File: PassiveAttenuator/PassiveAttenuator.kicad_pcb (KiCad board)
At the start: 2 copper layers, 15 x 100 mm, 6 parts, among them J1 AudioJack2_SwitchT, J2 AudioJack2_SwitchT, J3 AudioJack2_SwitchT, J4 AudioJack2_SwitchT

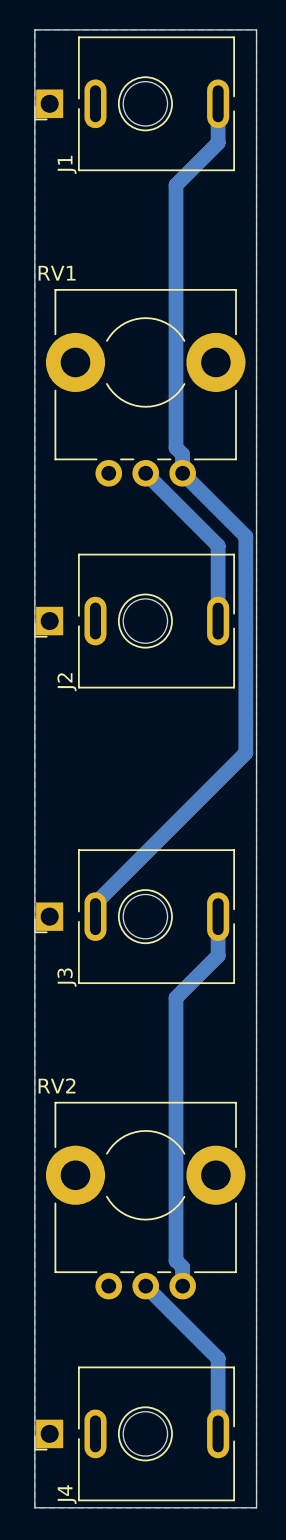
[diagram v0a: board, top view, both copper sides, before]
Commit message: Moved potentiometers to top.
Add top layer gnd pour
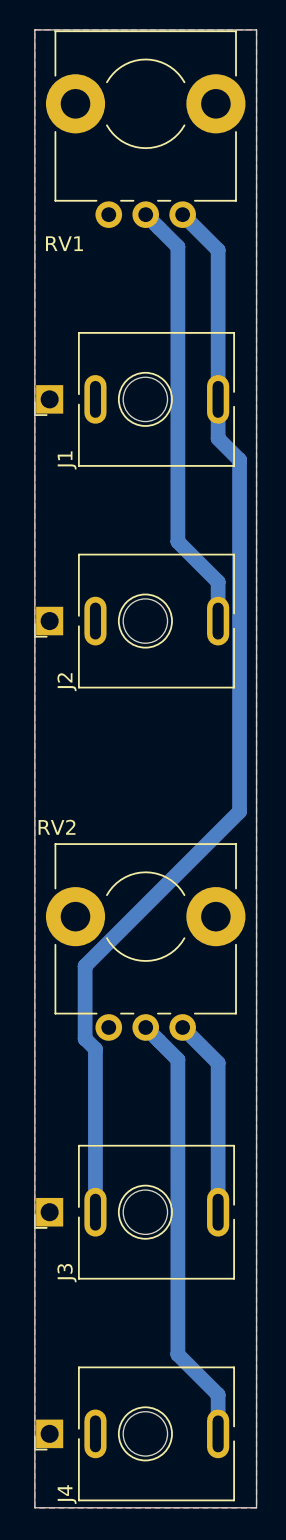
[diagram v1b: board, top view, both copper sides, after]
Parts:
- moved J1 20.0 mm to (151.0, 75.0)
- moved J3 20.0 mm to (151.0, 130.0)
- moved RV1 17.5 mm to (160.0, 62.5)
- moved RV2 17.5 mm to (160.0, 117.5)
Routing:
- net Net-(J4-PadT): track 12.0 -> 29.5 mm
- net Net-(J2-PadT): track 12.0 -> 29.5 mm
- net Net-(J3-PadT): track 26.4 -> 13.5 mm
- net Net-(J1-PadT): track 62.4 -> 73.7 mm
- added copper zone on F.Cu, net GND
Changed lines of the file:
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@@
     (thickness 1.6)
     (drawings 4)
-    (tracks 18)
+    (tracks 21)
     (zones 0)
     (modules 6)
@@
     (solder_mask_min_width 0.25)
     (aux_axis_origin 0 0)
-    (visible_elements FFFFFF7F)
+    (visible_elements 7FFFFFFF)
     (pcbplotparams
       (layerselection 0x010fc_ffffffff)
@@
   )
   (module _NTSFootprints:Jack_3.5mm_QingPu_WQP-PJ398SM_Vertical_CenterHole_OvalPads (layer F.Cu)
-    (at 151 55 90)
+    (at 151 75 90)
     (descr "TRS 3.5mm, vertical, Thonkiconn, PCB mount, (http://www.qingpu-electronics.com/en/products/WQP-PJ398SM-362.html)")
     (tags "WQP-PJ398SM WQP-PJ301M-12 TRS 3.5mm mono vertical jack thonkiconn qingpu")
@@
   )
   (module _NTSFootprints:Jack_3.5mm_QingPu_WQP-PJ398SM_Vertical_CenterHole_OvalPads (layer F.Cu)
-    (at 151 110 90)
+    (at 151 130 90)
     (descr "TRS 3.5mm, vertical, Thonkiconn, PCB mount, (http://www.qingpu-electronics.com/en/products/WQP-PJ398SM-362.html)")
     (tags "WQP-PJ398SM WQP-PJ301M-12 TRS 3.5mm mono vertical jack thonkiconn qingpu")
@@
   )
   (module _NTSFootprints:Potentiometer_Alps_RK09L_Plated_Mount_Holes (layer F.Cu)
-    (at 160 80 90)
+    (at 160 62.5 90)
     (descr "Potentiometer, horizontally mounted, Omeg PC16PU, Omeg PC16PU, Omeg PC16PU, Vishay/Spectrol 248GJ/249GJ Single, Vishay/Spectrol 248GJ/249GJ Single, Vishay/Spectrol 248GJ/249GJ Single, Vishay/Spectrol 248GH/249GH Single, Vishay/Spectrol 148/149 Single, Vishay/Spectrol 148/149 Single, Vishay/Spectrol 148/149 Single, Vishay/Spectrol 148A/149A Single with mounting plates, Vishay/Spectrol 148/149 Double, Vishay/Spectrol 148A/149A Double with mounting plates, Piher PC-16 Single, Piher PC-16 Single, Piher PC-16 Single, Piher PC-16SV Single, Piher PC-16 Double, Piher PC-16 Triple, Piher T16H Single, Piher T16L Single, Piher T16H Double, Alps RK163 Single, Alps RK163 Double, Alps RK097 Single, Alps RK097 Double, Bourns PTV09A-2 Single with mounting sleve Single, Bourns PTV09A-1 with mounting sleve Single, Bourns PRS11S Single, Alps RK09K Single with mounting sleve Single, Alps RK09K with mounting sleve Single, Alps RK09L Single, Alps RK09L Single, http://www.alps.com/prod/info/E/HTML/Potentiometer/RotaryPotentiometers/RK09L/RK09L1140A5E.html")
     (tags "Potentiometer horizontal  Omeg PC16PU  Omeg PC16PU  Omeg PC16PU  Vishay/Spectrol 248GJ/249GJ Single  Vishay/Spectrol 248GJ/249GJ Single  Vishay/Spectrol 248GJ/249GJ Single  Vishay/Spectrol 248GH/249GH Single  Vishay/Spectrol 148/149 Single  Vishay/Spectrol 148/149 Single  Vishay/Spectrol 148/149 Single  Vishay/Spectrol 148A/149A Single with mounting plates  Vishay/Spectrol 148/149 Double  Vishay/Spectrol 148A/149A Double with mounting plates  Piher PC-16 Single  Piher PC-16 Single  Piher PC-16 Single  Piher PC-16SV Single  Piher PC-16 Double  Piher PC-16 Triple  Piher T16H Single  Piher T16L Single  Piher T16H Double  Alps RK163 Single  Alps RK163 Double  Alps RK097 Single  Alps RK097 Double  Bourns PTV09A-2 Single with mounting sleve Single  Bourns PTV09A-1 with mounting sleve Single  Bourns PRS11S Single  Alps RK09K Single with mounting sleve Single  Alps RK09K with mounting sleve Single  Alps RK09L Single  Alps RK09L Single")
-    (fp_text reference RV1 (at 13.5 -8.5 180) (layer F.SilkS)
-      (effects (font (size 1 1) (thickness 0.15)))
-    )
-    (fp_text value R_POT (at 13.5 -4 180) (layer F.Fab) hide
+    (fp_text reference RV1 (at -2 -8 180) (layer F.SilkS)
+      (effects (font (size 1 1) (thickness 0.15)))
+    )
+    (fp_text value R_POT (at 8 -2.5 180) (layer F.Fab) hide
       (effects (font (size 1 1) (thickness 0.15)))
     )
@@
   )
   (module _NTSFootprints:Potentiometer_Alps_RK09L_Plated_Mount_Holes (layer F.Cu)
-    (at 160 135 90)
+    (at 160 117.5 90)
     (descr "Potentiometer, horizontally mounted, Omeg PC16PU, Omeg PC16PU, Omeg PC16PU, Vishay/Spectrol 248GJ/249GJ Single, Vishay/Spectrol 248GJ/249GJ Single, Vishay/Spectrol 248GJ/249GJ Single, Vishay/Spectrol 248GH/249GH Single, Vishay/Spectrol 148/149 Single, Vishay/Spectrol 148/149 Single, Vishay/Spectrol 148/149 Single, Vishay/Spectrol 148A/149A Single with mounting plates, Vishay/Spectrol 148/149 Double, Vishay/Spectrol 148A/149A Double with mounting plates, Piher PC-16 Single, Piher PC-16 Single, Piher PC-16 Single, Piher PC-16SV Single, Piher PC-16 Double, Piher PC-16 Triple, Piher T16H Single, Piher T16L Single, Piher T16H Double, Alps RK163 Single, Alps RK163 Double, Alps RK097 Single, Alps RK097 Double, Bourns PTV09A-2 Single with mounting sleve Single, Bourns PTV09A-1 with mounting sleve Single, Bourns PRS11S Single, Alps RK09K Single with mounting sleve Single, Alps RK09K with mounting sleve Single, Alps RK09L Single, Alps RK09L Single, http://www.alps.com/prod/info/E/HTML/Potentiometer/RotaryPotentiometers/RK09L/RK09L1140A5E.html")
     (tags "Potentiometer horizontal  Omeg PC16PU  Omeg PC16PU  Omeg PC16PU  Vishay/Spectrol 248GJ/249GJ Single  Vishay/Spectrol 248GJ/249GJ Single  Vishay/Spectrol 248GJ/249GJ Single  Vishay/Spectrol 248GH/249GH Single  Vishay/Spectrol 148/149 Single  Vishay/Spectrol 148/149 Single  Vishay/Spectrol 148/149 Single  Vishay/Spectrol 148A/149A Single with mounting plates  Vishay/Spectrol 148/149 Double  Vishay/Spectrol 148A/149A Double with mounting plates  Piher PC-16 Single  Piher PC-16 Single  Piher PC-16 Single  Piher PC-16SV Single  Piher PC-16 Double  Piher PC-16 Triple  Piher T16H Single  Piher T16L Single  Piher T16H Double  Alps RK163 Single  Alps RK163 Double  Alps RK097 Single  Alps RK097 Double  Bourns PTV09A-2 Single with mounting sleve Single  Bourns PTV09A-1 with mounting sleve Single  Bourns PRS11S Single  Alps RK09K Single with mounting sleve Single  Alps RK09K with mounting sleve Single  Alps RK09L Single  Alps RK09L Single")
@@
   (gr_line (start 150 150) (end 165 150) (layer Edge.Cuts) (width 0.05))
   (gr_line (start 150 50) (end 150 150) (layer Edge.Cuts) (width 0.05))
-  (segment (start 160 78.727208) (end 160 80) (width 1) (layer B.Cu) (net 1))
-  (segment (start 159.549999 78.277207) (end 160 78.727208) (width 1) (layer B.Cu) (net 1))
-  (segment (start 159.549999 60.500001) (end 159.549999 78.277207) (width 1) (layer B.Cu) (net 1))
-  (segment (start 162.4 57.65) (end 159.549999 60.500001) (width 1) (layer B.Cu) (net 1))
-  (segment (start 162.4 55) (end 162.4 57.65) (width 1) (layer B.Cu) (net 1))
-  (segment (start 154.1 109.1) (end 154.1 110) (width 1) (layer B.Cu) (net 1))
-  (segment (start 164.27499 98.92501) (end 154.1 109.1) (width 1) (layer B.Cu) (net 1))
-  (segment (start 164.27499 84.27499) (end 164.27499 98.92501) (width 1) (layer B.Cu) (net 1))
-  (segment (start 160 80) (end 164.27499 84.27499) (width 1) (layer B.Cu) (net 1))
-  (segment (start 162.4 84.9) (end 157.5 80) (width 1) (layer B.Cu) (net 5))
-  (segment (start 162.4 90) (end 162.4 84.9) (width 1) (layer B.Cu) (net 5))
-  (segment (start 162.4 112.65) (end 162.4 110) (width 1) (layer B.Cu) (net 6))
-  (segment (start 159.549999 115.500001) (end 162.4 112.65) (width 1) (layer B.Cu) (net 6))
-  (segment (start 159.549999 133.277207) (end 159.549999 115.500001) (width 1) (layer B.Cu) (net 6))
-  (segment (start 160 133.727208) (end 159.549999 133.277207) (width 1) (layer B.Cu) (net 6))
-  (segment (start 160 135) (end 160 133.727208) (width 1) (layer B.Cu) (net 6))
-  (segment (start 162.4 139.9) (end 157.5 135) (width 1) (layer B.Cu) (net 8))
-  (segment (start 162.4 145) (end 162.4 139.9) (width 1) (layer B.Cu) (net 8))
+  (segment (start 162.4 64.9) (end 160 62.5) (width 1) (layer B.Cu) (net 1))
+  (segment (start 162.4 75) (end 162.4 64.9) (width 1) (layer B.Cu) (net 1))
+  (segment (start 163.85001 79.10001) (end 162.4 77.65) (width 1) (layer B.Cu) (net 1))
+  (segment (start 163.85001 102.895992) (end 163.85001 79.10001) (width 1) (layer B.Cu) (net 1))
+  (segment (start 162.4 77.65) (end 162.4 75) (width 1) (layer B.Cu) (net 1))
+  (segment (start 153.399999 113.346003) (end 163.85001 102.895992) (width 1) (layer B.Cu) (net 1))
+  (segment (start 153.399999 118.268001) (end 153.399999 113.346003) (width 1) (layer B.Cu) (net 1))
+  (segment (start 154.1 118.968002) (end 153.399999 118.268001) (width 1) (layer B.Cu) (net 1))
+  (segment (start 154.1 130) (end 154.1 118.968002) (width 1) (layer B.Cu) (net 1))
+  (segment (start 158.399999 63.399999) (end 157.5 62.5) (width 1) (layer B.Cu) (net 5))
+  (segment (start 159.677001 64.677001) (end 158.399999 63.399999) (width 1) (layer B.Cu) (net 5))
+  (segment (start 159.677001 84.627001) (end 159.677001 64.677001) (width 1) (layer B.Cu) (net 5))
+  (segment (start 162.4 87.35) (end 159.677001 84.627001) (width 1) (layer B.Cu) (net 5))
+  (segment (start 162.4 90) (end 162.4 87.35) (width 1) (layer B.Cu) (net 5))
+  (segment (start 162.4 119.9) (end 160 117.5) (width 1) (layer B.Cu) (net 6))
+  (segment (start 162.4 130) (end 162.4 119.9) (width 1) (layer B.Cu) (net 6))
+  (segment (start 158.399999 118.399999) (end 157.5 117.5) (width 1) (layer B.Cu) (net 8))
+  (segment (start 159.677001 119.677001) (end 158.399999 118.399999) (width 1) (layer B.Cu) (net 8))
+  (segment (start 159.677001 139.627001) (end 159.677001 119.677001) (width 1) (layer B.Cu) (net 8))
+  (segment (start 162.4 142.35) (end 159.677001 139.627001) (width 1) (layer B.Cu) (net 8))
+  (segment (start 162.4 145) (end 162.4 142.35) (width 1) (layer B.Cu) (net 8))
   (zone (net 2) (net_name GND) (layer B.Cu) (hatch edge 0.508)
     (connect_pads (clearance 0.508))
     (min_thickness 0.254)
+    (fill yes (arc_segments 32) (thermal_gap 0.508) (thermal_bridge_width 0.508))
+    (polygon
+      (pts
+        (xy 150 50) (xy 165 50) (xy 165 150) (xy 150 150)
+      )
+    )
+  )
+  (zone (net 2) (net_name GND) (layer F.Cu) (hatch edge 0.508)
+    (connect_pads (clearance 0.508))
+    (min_thickness 0.254)

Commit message: Generate gerbers and step
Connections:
- RV1 pad : (no net) -> GND
- RV2 pad : (no net) -> GND
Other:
- board text added: "Passive Attenuator v1.0"
- board text added: "schenktronics.com"

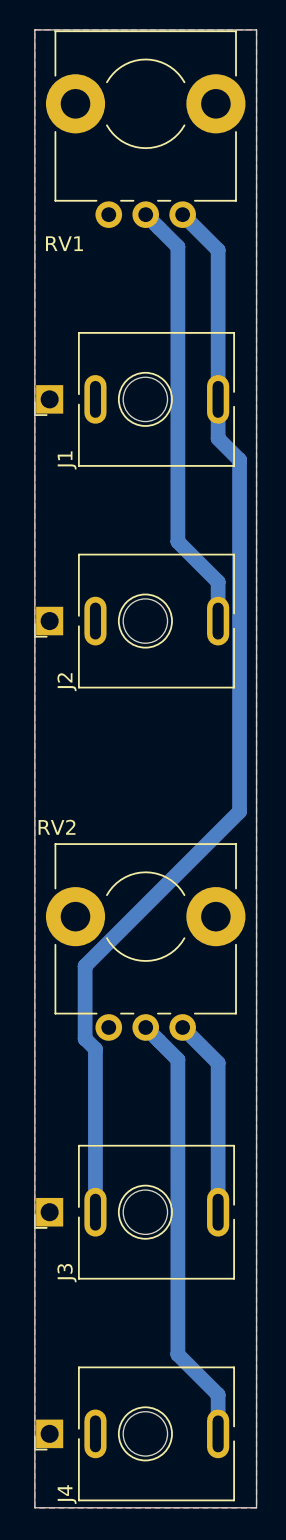
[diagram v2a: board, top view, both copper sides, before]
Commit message: Move jacks to center
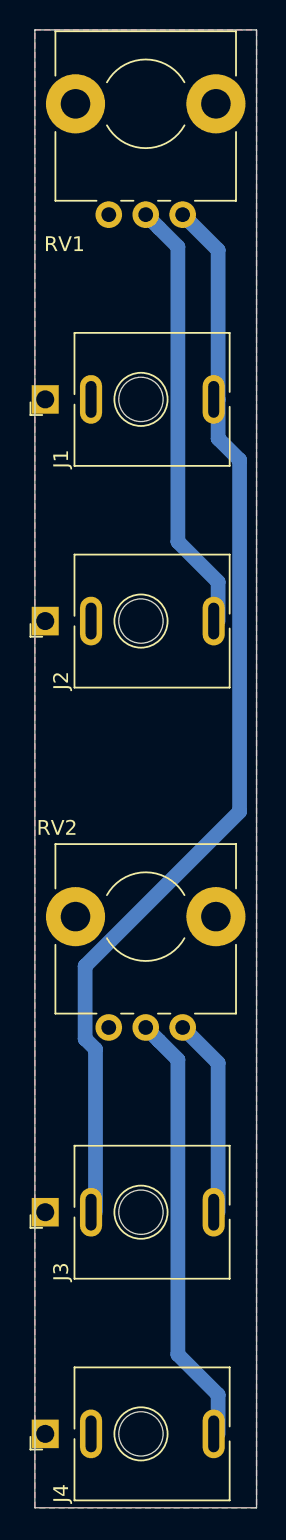
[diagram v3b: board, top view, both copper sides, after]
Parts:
- moved J1 0.30 mm to (150.7, 75.0)
- moved J2 0.30 mm to (150.7, 90.0)
- moved J3 0.30 mm to (150.7, 130.0)
- moved J4 0.30 mm to (150.7, 145.0)
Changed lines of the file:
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@@
   )
   (module _NTSFootprints:Jack_3.5mm_QingPu_WQP-PJ398SM_Vertical_CenterHole_OvalPads (layer F.Cu)
-    (at 151 75 90)
+    (at 150.7 75 90)
     (descr "TRS 3.5mm, vertical, Thonkiconn, PCB mount, (http://www.qingpu-electronics.com/en/products/WQP-PJ398SM-362.html)")
     (tags "WQP-PJ398SM WQP-PJ301M-12 TRS 3.5mm mono vertical jack thonkiconn qingpu")
@@
   )
   (module _NTSFootprints:Jack_3.5mm_QingPu_WQP-PJ398SM_Vertical_CenterHole_OvalPads (layer F.Cu)
-    (at 151 90 90)
+    (at 150.7 90 90)
     (descr "TRS 3.5mm, vertical, Thonkiconn, PCB mount, (http://www.qingpu-electronics.com/en/products/WQP-PJ398SM-362.html)")
     (tags "WQP-PJ398SM WQP-PJ301M-12 TRS 3.5mm mono vertical jack thonkiconn qingpu")
@@
   )
   (module _NTSFootprints:Jack_3.5mm_QingPu_WQP-PJ398SM_Vertical_CenterHole_OvalPads (layer F.Cu)
-    (at 151 130 90)
+    (at 150.7 130 90)
     (descr "TRS 3.5mm, vertical, Thonkiconn, PCB mount, (http://www.qingpu-electronics.com/en/products/WQP-PJ398SM-362.html)")
     (tags "WQP-PJ398SM WQP-PJ301M-12 TRS 3.5mm mono vertical jack thonkiconn qingpu")
@@
   )
   (module _NTSFootprints:Jack_3.5mm_QingPu_WQP-PJ398SM_Vertical_CenterHole_OvalPads (layer F.Cu)
-    (at 151 145 90)
+    (at 150.7 145 90)
     (descr "TRS 3.5mm, vertical, Thonkiconn, PCB mount, (http://www.qingpu-electronics.com/en/products/WQP-PJ398SM-362.html)")
     (tags "WQP-PJ398SM WQP-PJ301M-12 TRS 3.5mm mono vertical jack thonkiconn qingpu")
